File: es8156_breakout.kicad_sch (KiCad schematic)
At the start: 9 parts, among them J1 Headphones, J2 Conn_01x12, J3 Conn_01x03, U1 ES8156

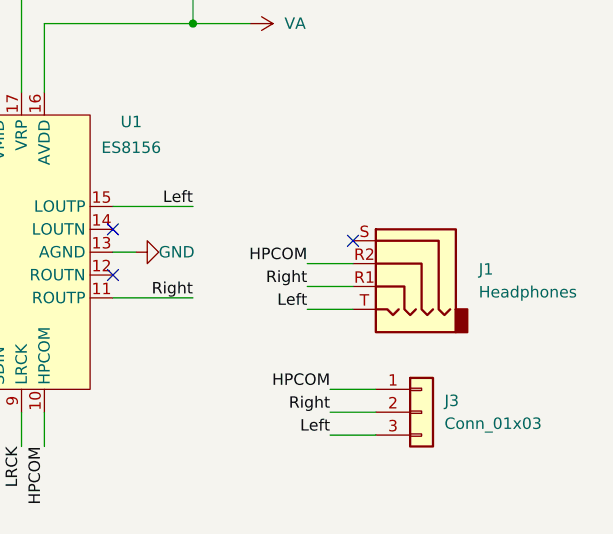
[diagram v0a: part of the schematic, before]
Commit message: use lcsc imported audio jack
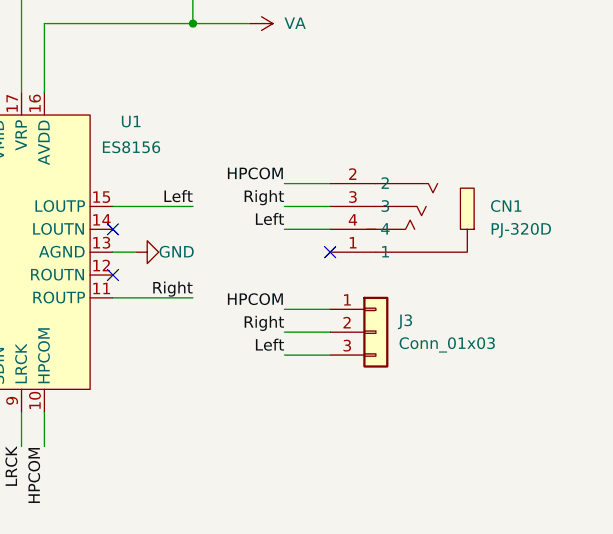
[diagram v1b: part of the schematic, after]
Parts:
- removed J1: Headphones, Connector_Audio:Jack_3.5mm_PJ320D_Horizontal, symbol Connector_Audio:AudioJack4
- added CN1: PJ-320D, lcsc_parts:AUDIO-SMD_PJ-320D, symbol lcsc:PJ-320D
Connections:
- net HPCOM: now also CN1.2
- net Left: now also CN1.4
- net Right: now also CN1.3
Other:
- moved on the sheet: J3
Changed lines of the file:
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@@
+	)
+	(no_connect
+		(at 146.05 97.79)
 	)
 	(no_connect
@@
 		(at 121.92 100.33)
 	)
-	(no_connect
-		(at 148.59 96.52)
-	)
-	(wire
-		(pts
-			(xy 143.51 104.14) (xy 148.59 104.14)
-		)
-		(stroke
-			(width 0)
-			(type default)
-		)
-	)
 	(wire
 		(pts
@@
 	(wire
 		(pts
-			(xy 146.05 115.57) (xy 151.13 115.57)
+			(xy 140.97 106.68) (xy 146.05 106.68)
+		)
+		(stroke
+			(width 0)
+			(type default)
+		)
+	)
+	(wire
+		(pts
+			(xy 140.97 90.17) (xy 146.05 90.17)
 		)
 		(stroke
@@
 	(wire
 		(pts
-			(xy 143.51 99.06) (xy 148.59 99.06)
-		)
-		(stroke
-			(width 0)
-			(type default)
-		)
-	)
-	(wire
-		(pts
 			(xy 74.93 53.34) (xy 74.93 55.88)
 		)
@@
 	(wire
 		(pts
-			(xy 146.05 118.11) (xy 151.13 118.11)
+			(xy 140.97 109.22) (xy 146.05 109.22)
+		)
+		(stroke
+			(width 0)
+			(type default)
+		)
+	)
+	(wire
+		(pts
+			(xy 140.97 95.25) (xy 146.05 95.25)
 		)
 		(stroke
@@
 	(wire
 		(pts
-			(xy 146.05 113.03) (xy 151.13 113.03)
-		)
-		(stroke
-			(width 0)
-			(type default)
-		)
-	)
-	(wire
-		(pts
-			(xy 143.51 101.6) (xy 148.59 101.6)
+			(xy 140.97 104.14) (xy 146.05 104.14)
 		)
 		(stroke
@@
 		(pts
 			(xy 130.81 64.77) (xy 130.81 72.39)
+		)
+		(stroke
+			(width 0)
+			(type default)
+		)
+	)
+	(wire
+		(pts
+			(xy 140.97 92.71) (xy 146.05 92.71)
 		)
 		(stroke
@@
 		)
 	)
-	(label "Right"
-		(at 143.51 101.6 180)
+	(label "Left"
+		(at 140.97 95.25 180)
 		(effects
 			(font
@@
 	)
 	(label "Right"
-		(at 146.05 115.57 180)
+		(at 140.97 106.68 180)
 		(effects
 			(font
@@
 	)
 	(label "HPCOM"
-		(at 146.05 113.03 180)
-		(effects
-			(font
-				(size 1.27 1.27)
-			)
-			(justify right bottom)
-		)
-	)
-	(label "HPCOM"
-		(at 143.51 99.06 180)
+		(at 140.97 104.14 180)
 		(effects
 			(font
@@
 	)
 	(label "Left"
-		(at 146.05 118.11 180)
+		(at 140.97 109.22 180)
 		(effects
 			(font
@@
 		)
 	)
-	(label "Left"
-		(at 143.51 104.14 180)
+	(label "Right"
+		(at 140.97 92.71 180)
 		(effects
 			(font
@@
 	(label "MCLK"
 		(at 77.47 66.04 180)
+		(effects
+			(font
+				(size 1.27 1.27)
+			)
+			(justify right bottom)
+		)
+	)
+	(label "HPCOM"
+		(at 140.97 90.17 180)
 		(effects
 			(font
@@
 	)
 	(symbol
+		(lib_id "lcsc:PJ-320D")
+		(at 151.13 95.25 180)
+		(unit 1)
+		(exclude_from_sim no)
+		(in_bom yes)
+		(on_board yes)
+		(dnp no)
+		(fields_autoplaced yes)
+		(property "Reference" "CN1"
+			(at 163.83 92.7099 0)
+			(effects
+				(font
+					(size 1.27 1.27)
+				)
+				(justify right)
+			)
+		)
+		(property "Value" "PJ-320D"
+			(at 163.83 95.2499 0)
+			(effects
+				(font
+					(size 1.27 1.27)
+				)
+				(justify right)
+			)
+		)
+		(property "Footprint" "lcsc_parts:AUDIO-SMD_PJ-320D"
+			(at 151.13 82.55 0)
+			(effects
+				(font
+					(size 1.27 1.27)
+				)
+				(hide yes)
+			)
+		)
+		(property "Datasheet" "https://lcsc.com/product-detail/Audio-Video-Connectors_SHOU-HAN-PJ-320D_C431535.html"
+			(at 151.13 80.01 0)
+			(effects
+				(font
+					(size 1.27 1.27)
+				)
+				(hide yes)
+			)
+		)
+		(property "Description" ""
+			(at 151.13 95.25 0)
+			(effects
+				(font
+					(size 1.27 1.27)
+				)
+				(hide yes)
+			)
+		)
+		(property "LCSC Part" "C431535"
+			(at 151.13 77.47 0)
+			(effects
+				(font
+					(size 1.27 1.27)
+				)
+				(hide yes)
+			)
+		)
+		(pin "3"
+		)
+		(pin "4"
+		)
+		(pin "2"
+		)
+		(pin "1"
+		)
+		(instances
+			(project ""
+				(path "/f82e772e-e40e-43f0-8dee-b43598452bf9"
+					(reference "CN1")
+					(unit 1)
+				)
+			)
+		)
+	)
+	(symbol
 		(lib_id "power:GND")
 		(at 124.46 97.79 90)
@@
 	)
 	(symbol
-		(lib_id "Connector_Audio:AudioJack4")
-		(at 153.67 99.06 0)
-		(mirror y)
-		(unit 1)
-		(exclude_from_sim no)
-		(in_bom yes)
-		(on_board yes)
-		(dnp no)
-		(fields_autoplaced yes)
-		(property "Reference" "J1"
-			(at 162.56 99.6949 0)
-			(effects
-				(font
-					(size 1.27 1.27)
-				)
-				(justify right)
-			)
-		)
-		(property "Value" "Headphones"
-			(at 162.56 102.2349 0)
-			(effects
-				(font
-					(size 1.27 1.27)
-				)
-				(justify right)
-			)
-		)
-		(property "Footprint" "Connector_Audio:Jack_3.5mm_PJ320D_Horizontal"
-			(at 153.67 99.06 0)
-			(effects
-				(font
-					(size 1.27 1.27)
-				)
-				(hide yes)
-			)
-		)
-		(property "Datasheet" "~"
-			(at 153.67 99.06 0)
-			(effects
-				(font
-					(size 1.27 1.27)
-				)
-				(hide yes)
-			)
-		)
-		(property "Description" "Audio Jack, 4 Poles (TRRS)"
-			(at 153.67 99.06 0)
-			(effects
-				(font
-					(size 1.27 1.27)
-				)
-				(hide yes)
-			)
-		)
-		(pin "T"
-		)
-		(pin "S"
-		)
-		(pin "R1"
-		)
-		(pin "R2"
-		)
-		(instances
-			(project ""
-				(path "/f82e772e-e40e-43f0-8dee-b43598452bf9"
-					(reference "J1")
-					(unit 1)
-				)
-			)
-		)
-	)
-	(symbol
 		(lib_id "power:GND")
 		(at 74.93 53.34 180)
@@
 	(symbol
 		(lib_id "Connector_Generic:Conn_01x03")
-		(at 156.21 115.57 0)
+		(at 151.13 106.68 0)
 		(unit 1)
 		(exclude_from_sim no)
@@
 		(fields_autoplaced yes)
 		(property "Reference" "J3"
-			(at 158.75 114.2999 0)
+			(at 153.67 105.4099 0)
 			(effects
 				(font
@@
 		)
 		(property "Value" "Conn_01x03"
-			(at 158.75 116.8399 0)
+			(at 153.67 107.9499 0)
 			(effects
 				(font
@@
 		)
 		(property "Footprint" "Connector_PinHeader_2.54mm:PinHeader_1x03_P2.54mm_Vertical"
-			(at 156.21 115.57 0)
+			(at 151.13 106.68 0)
 			(effects
 				(font
@@
 		)
 		(property "Datasheet" "~"
-			(at 156.21 115.57 0)
+			(at 151.13 106.68 0)
 			(effects
 				(font
@@
 		)
 		(property "Description" "Generic connector, single row, 01x03, script generated (kicad-library-utils/schlib/autogen/connector/)"
-			(at 156.21 115.57 0)
-			(effects
-				(font
+			(at 151.13 106.68 0)
+			(effects
+				(font
